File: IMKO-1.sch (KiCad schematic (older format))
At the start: 108 parts, among them J1 CONN_POWER, J2 CONN_EXPANSION, J9 CONN_VIDEO, P1 CONN_KBD, T3 CONN_6, T4 CONN_1, U1 8080, U11 2114, U12 2114, U13 74LS374, U14 74LS165, U15 74LS244, U16 74LS244, U17 74LS367, U18 82S129, U19 74LS244, U2 8228, U20 74LS244, U21 74LS08, U22 74LS32, U23 74LS86, U24 74LS163, U25 74LS00, U26 74LS374, U27 2114, U28 2114, U29 2114, U3 8224, U30 2114, U31 2114, U32 2114, U33 74LS138, U34 74LS32, U35 74LS00, U36 74LS240, U37 74LS148, U38 74LS244, U39 74LS244, U4 2708, U40 74LS244, U41 74LS245, U49 74LS244, U5 2708, U55 DIL20, U6 2708, U7 2708, U8 SFF96364, U9 RO-3-2513, X1 18MHz, X2 1MHz

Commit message: Schematics cleanup, renamed signals
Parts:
- VR1: value POT -> ?
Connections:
- net labels added: ASCII.A0, ASCII.A1, ASCII.A2, ASCII.A3, ASCII.A4, ASCII.A5, ASCII.A6, CHR.ROW0, CHR.ROW1, CHR.ROW2, CS.ROM0, CS.ROM1, CS.ROM2, CS.ROM3, CS.VRAM, CYR.DOT0, CYR.DOT6, CYR.DOT7, CYR.INH, CYRILLIC, DOT0, DOT1, DOT2, DOT3, DOT4, DOT5, DOT6, DOT7, EXT.INT0, EXT.INT1, EXT.INT2, EXT.INT3, KBD.RESET, KBD3, KBD5, LATIN, LATIN.INH, SYNC.OUT, VIDEO.OUT, ~EXT.DATA
- net labels removed: CHR.A0, CHR.A1, CHR.A2, CHR.A3, CHR.A4, CHR.A5, CHR.D6, CHR.Q7, CHR0, CHR1, CHR2, CHR3, CHR4, CHR5, CHR6, CHR7, CS.CASS, KBD.RESIN, OUT.INH, SFF.RO0, SFF.RO1, SFF.RO2, TMP.V7, TODO.U35.1, TODO.U37.1, TODO.U37.2, TODO.U37.3, TODO.U37.4, U23.8, U55.11, U55.15, U55.6, U55.9, VSYNC
- wire segments 1057 -> 1048
- no-connect marks 26 -> 28
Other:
- note added: ""Interrupt Code -> Data Bus" Buffer"
- note added: ""Keyboard -> Data Bus" Buffer"
- note added: "13MHz Oscillator (?)"
- note added: "1:8 Frequency Divider"
- note added: "2MHz Clock Generator"
- note added: "Address Bus Buffers"
- note added: "CPU"
- note added: "Character Generator - Cyrillic (?)"
- note added: "Character Generator - Latin"
- note added: "Control Signals' Buffer"
- note added: "Interrupt Priority Encoder"
- note added: "Parallel to Serial Register"
- note added: "RAM: 3kbytes (6 chips of 1024x4-bit)"
- note added: "ROM & RAM Chip-select Decoder"
- note added: "ROM: 2/4kbytes (2/4 chips of 1024x8-bit)"
- note added: "System Controller & (Data) Bus Driver"
- note added: "TODO: Missing Transistor?!"
- note added: "TODO: Names for 3 & 5"
- note added: "Time Delay +\nDebouncing"
- note added: "Video + Sync Mixer (?)"
- note removed: "TODO: Inputs?!"
- note removed: "TODO: Name"
- note removed: "TODO: Signal names"
- moved on the sheet: C33, P1, R1, R2, R4, R5, U21B, U22C, U22D, U34A, U34B, U34C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

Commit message: Added IO-selector and U42
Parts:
- added C25: 10uF, symbol CP1
- added C32: 68uF, symbol CP1
- added U42: 74LS74, symbol 74LS74
- added U50, U53: 74LS32, symbol 74LS32
- added U51: 74LS02, symbol 74LS02
- added U52: 74LS42, symbol 74LS42
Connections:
- net labels added: A2|A6|A7, A3|A6|A7, A6|A7, WRITE.U26, WRITE.U46.13, WRITE.U46.4, WRITE.U48, ~CS.IO0, ~CS.IO1, ~CS.IO2, ~CS.IO3, ~CS.IO4, ~CS.IO5, ~CS.IO6, ~CS.IO7, ~CS.IO8, ~CS.RAM0, ~CS.RAM1, ~CS.RAM2, ~CS.ROM0, ~CS.ROM1, ~CS.ROM2, ~CS.ROM3, ~CS.VRAM, ~READ.KBD, ~READ.U47, ~READ.UART.16, ~READ.UART.18, ~WRITE.UART.23
- net labels removed: CS.RAM0, CS.RAM1, CS.RAM2, CS.ROM0, CS.ROM1, CS.ROM2, CS.ROM3, CS.VRAM, U51.10
- wire segments 1048 -> 1116
- no-connect marks 28 -> 36
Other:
- note added: "TODO: Name"
- moved on the sheet: J1

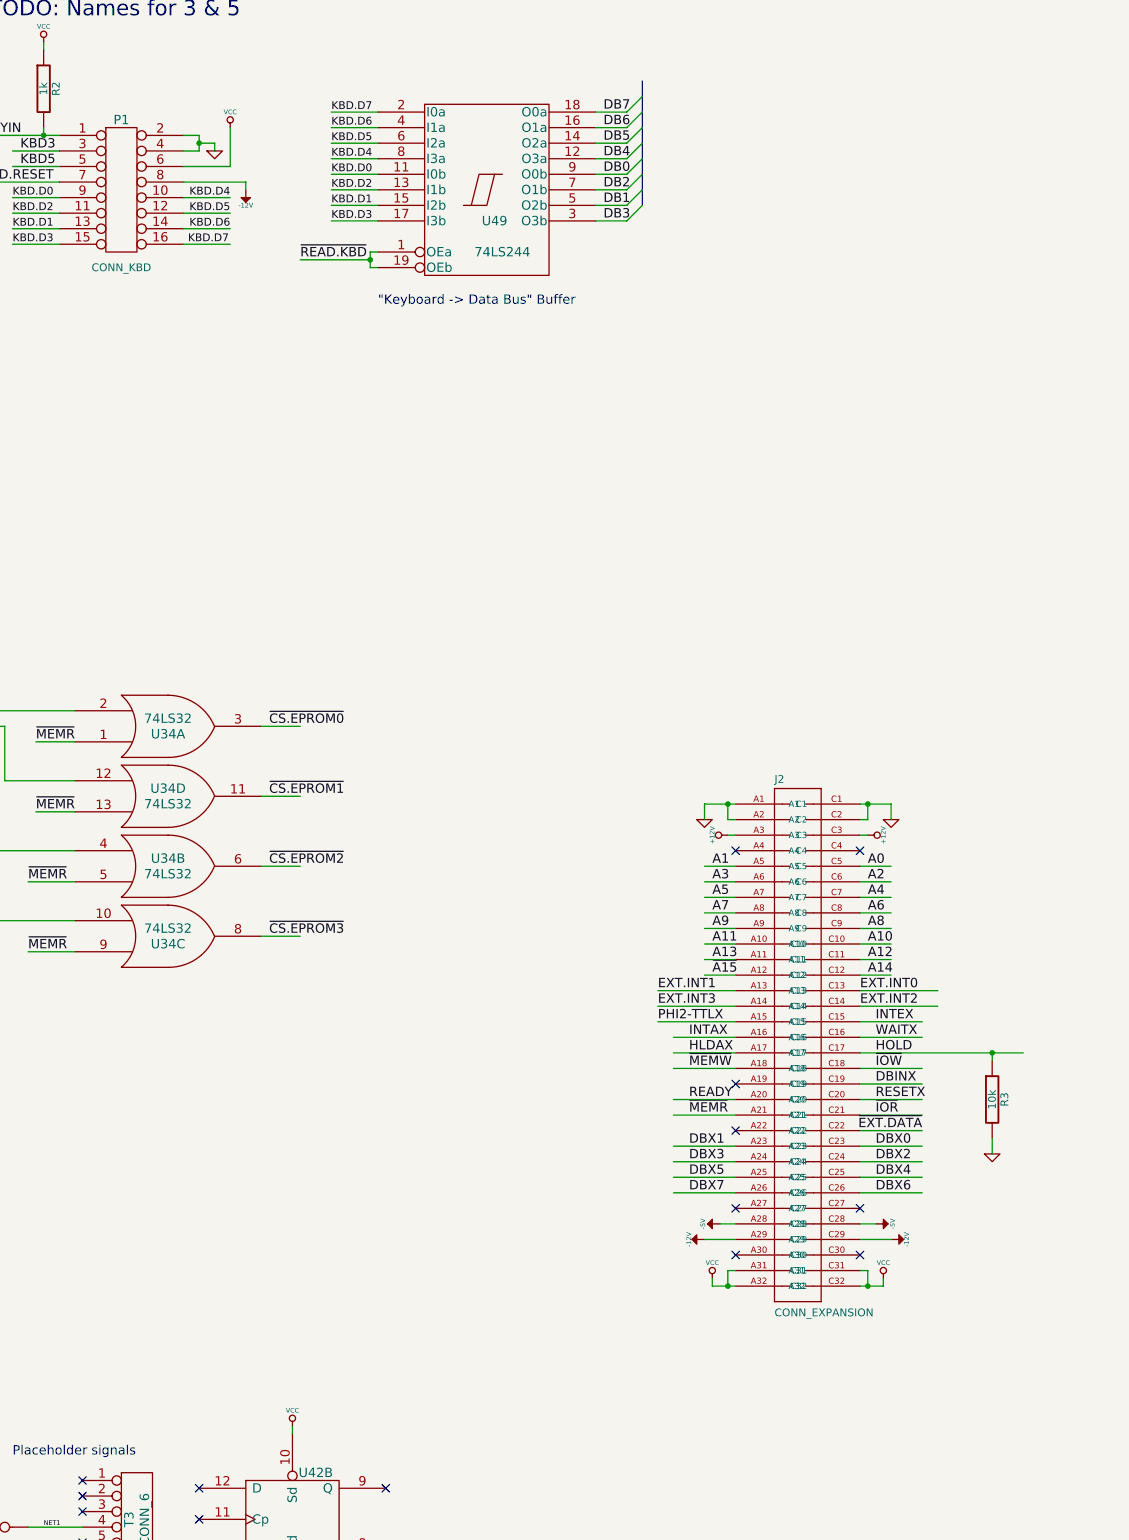
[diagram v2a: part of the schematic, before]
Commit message: Added external slot, completed PCB edges
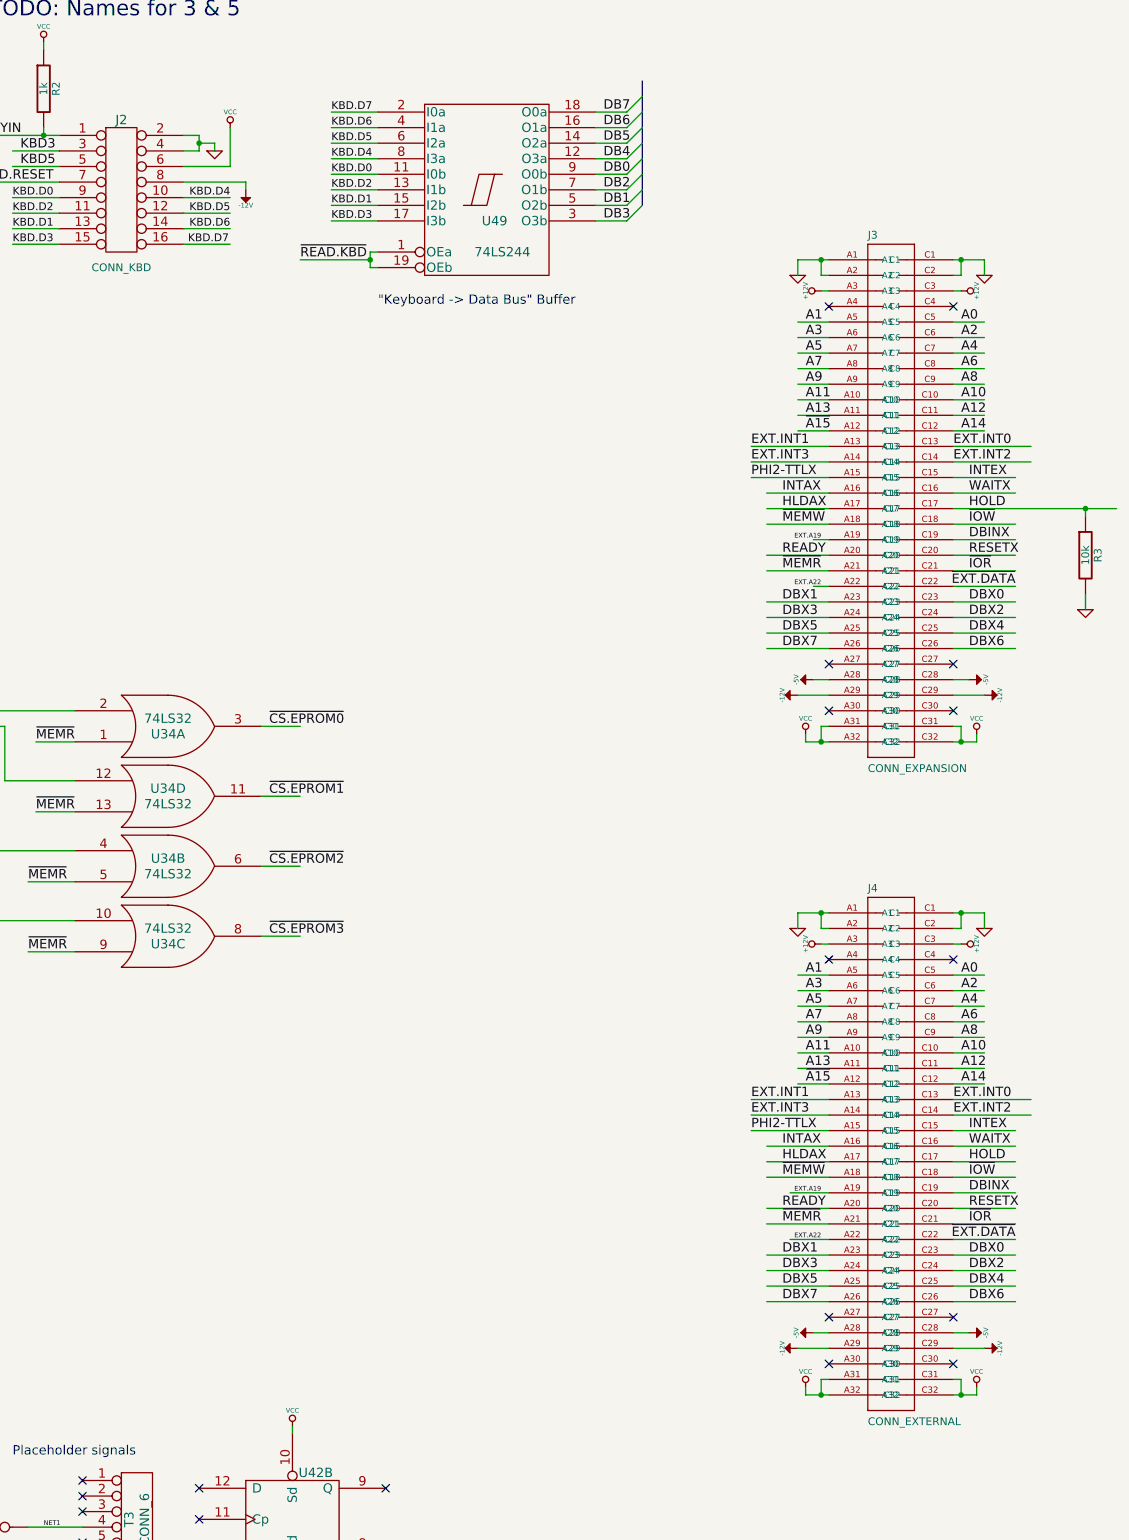
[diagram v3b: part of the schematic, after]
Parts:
- added J4: CONN_EXTERNAL, 19inch-VG64, symbol VG64
- renumbered P1 to J2, J2 to J3
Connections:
- net labels added: EXT.A19, EXT.A22
- wire segments 1116 -> 1184
- no-connect marks 36 -> 40
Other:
- moved on the sheet: J3, R3

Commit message: Added U10 UART and U42~48 ICs
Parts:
- added C28, C30, C31: 22nF, symbol C
- added C29: 150nF, symbol C
- added D4: 1N4148, symbol DIODE
- added J6: CONN_5, symbol CONN_5
- added J7, J8: DB9, symbol DB9
- added R44: 16k, symbol R
- added R45, R47: 1k, symbol R
- added R46: 39k, symbol R
- added U10: AY-5-1013A, oldchips-DIL40, symbol AY-5-1013A
- added U43: 74LS74, symbol 74LS74
- added U44: 74LS123, symbol 74LS123
- added U45: 74LS00, symbol 74LS00
- added U46: 74LS75, symbol 74LS75
- added U47: 74LS244, symbol 74LS244
- added U48: 74LS374, symbol 74LS374
- added U54: LM555N, symbol LM555N
- added VR2, VR3: ?, symbol POT
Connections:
- net labels added: IOR.D0, IOR.D1, IOR.D2, IOR.D3, IOR.D4, IOR.D5, IOR.D6, IOR.D7, IOW.D0, IOW.D1, IOW.D2, IOW.D3, IOW.D4, IOW.D5, IOW.D6, IOW.D7, NET2, U10.PULLUP, U44.1, U44.10, U44.13, U44.14, U44.15, U44.5, U44.6, U44.7, U46.Q0, U46.Q1, U46.Q3, U54.Q, UART.CLK, UART.IN, UART.OUT, WRITE.IO6, WRITE.IO7, ~READ.UART, ~READ.UART.STAT, ~UART.CLK.OUT, ~UART.OUT, ~WRITE.UART
- net labels removed: WRITE.U46.13, WRITE.U46.4, ~READ.UART.16, ~READ.UART.18, ~WRITE.UART.23
- wire segments 1184 -> 1369
- no-connect marks 40 -> 49
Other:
- note added: "IO6 and IO7 are at U46"
- moved on the sheet: U42B

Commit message: Added audio IO
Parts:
- added C22, C26: 10nF, symbol C
- added C23, C24: 15nF, symbol C
- added C27: 200pF, symbol C
- added D3: 1N4148, symbol DIODE
- added J5: CONN_5, symbol CONN_5
- added Q1, Q2: BC237, TO92-EBC, symbol BC237
- added Q3: BC558, TO92, symbol BC558
- added R35, R36: 22k, symbol R
- added R37, R42, R43: 11k, symbol R
- added R38, R39: 1k, symbol R
- added R40: 200k, symbol R
- added R41: 91k, symbol R
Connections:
- net labels added: AUDIO.CTRL1, AUDIO.CTRL2, AUDIO.IN, AUDIO.IN.AC, AUDIO.OUT, DIGITAL.IN
- net labels removed: U44.10
- wire segments 1369 -> 1413
- no-connect marks 49 -> 46
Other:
- note added: "UART Clock Generator ?"
- moved on the sheet: C28, R44, R45, U42B, U44B, VR2
